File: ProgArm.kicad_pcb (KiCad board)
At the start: 2 copper layers, 40 x 70 mm, 103 parts, among them J1 MICROSD_SOCKET_SPI, M1 MOTOR, P1 I2C_Port, P2 I2C_Solder, P3 SPI_Port, P4 SPI_Solder, P5 JTAG_Interface, P6 Unused_Pins, P7 HC-05/06, P8 Ring_Port, P9 MicroUSB, Q1 MOS_P, Q10 MOS_P, Q11 MOS_P, Q12 MOS_P, Q2 MOS_N, Q3 MOS_N, Q4 MOS_P, Q5 MOS_P, Q6 MOS_P, Q7 MOS_P, Q8 MOS_P, Q9 MOS_P, SW1 ON/OFF, SW2 SWITCH_INV, U1 STM32F103R, U2 LTC2942-1, U3 BMP085, U4 HMC5883L, U5 MPU6050, X1 32.768(MS3V-T1R), X2 8 mHz

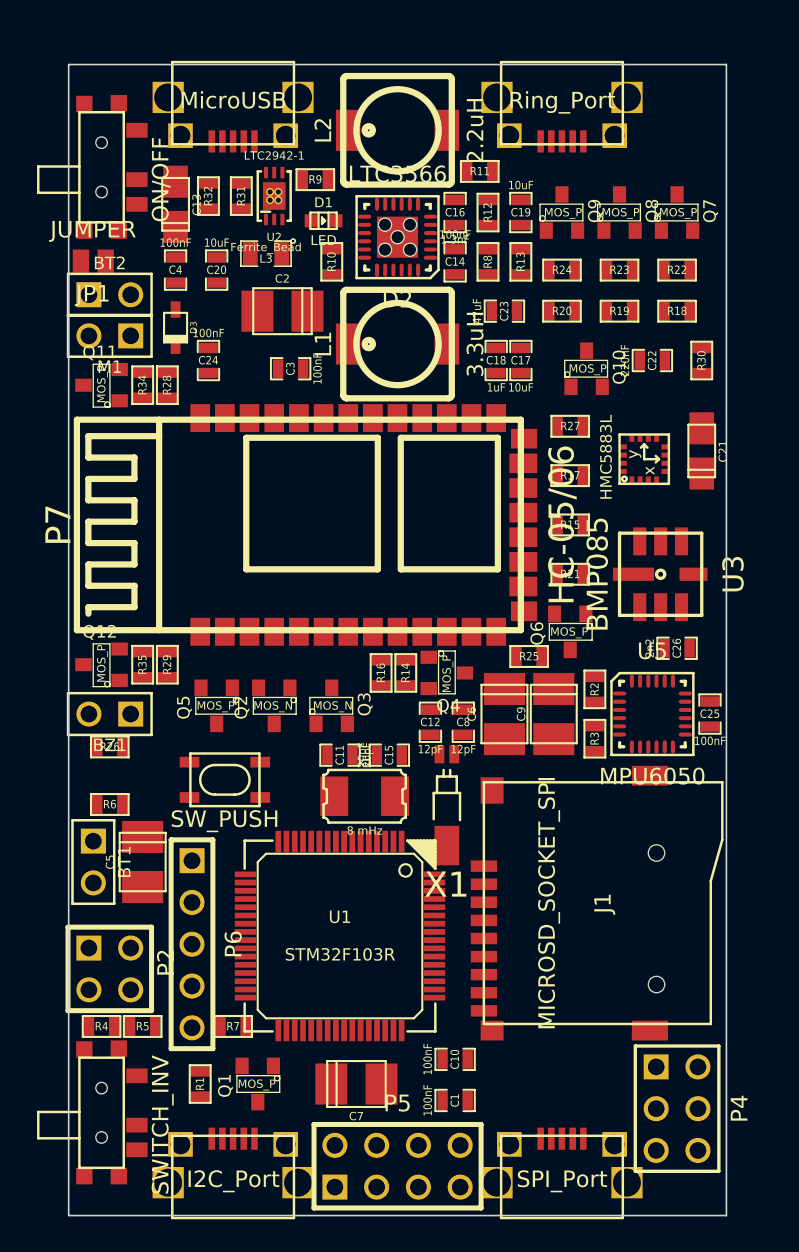
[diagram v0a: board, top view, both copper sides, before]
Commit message: Rearranged components
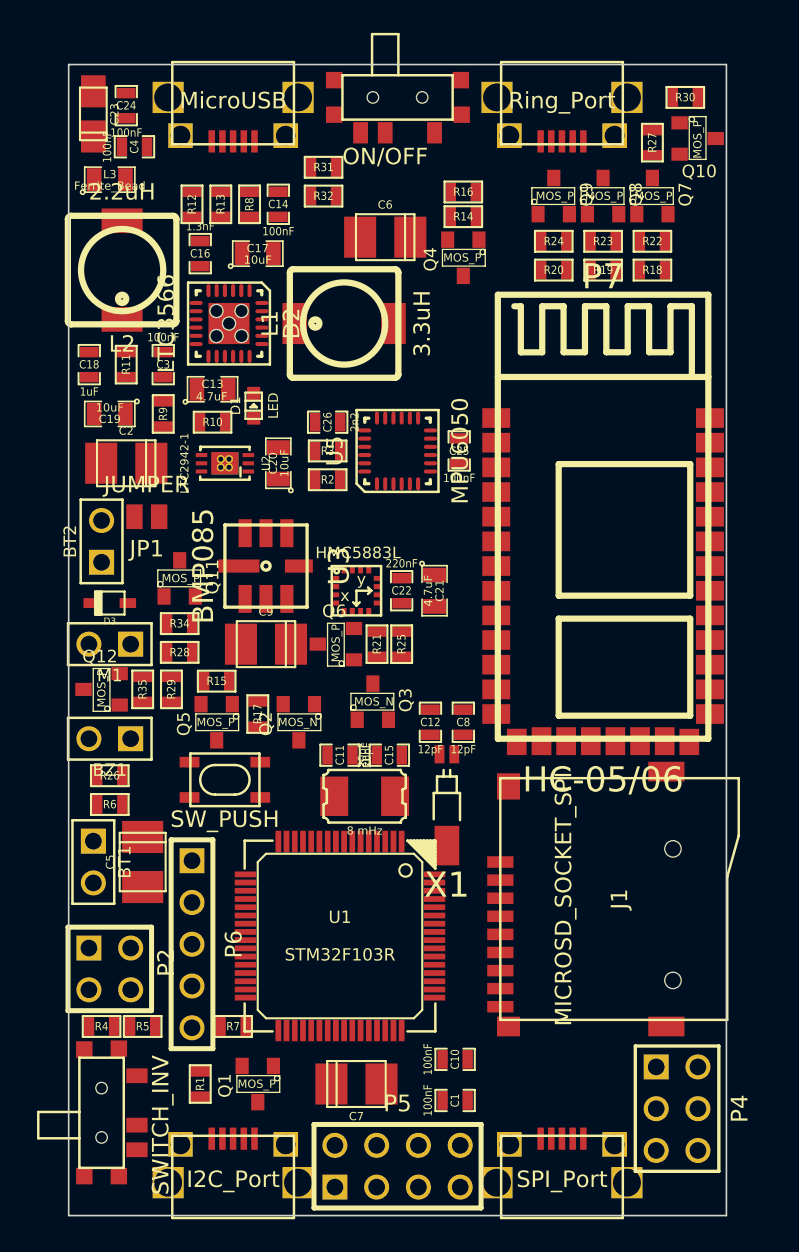
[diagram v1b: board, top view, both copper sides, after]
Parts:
- C13, C21: footprint c_tant_A -> SM0805
- C17, C19, C20: footprint SM0603_Capa -> SM0805
- C23: footprint SM0603_Capa -> c_tant_A
- moved C6 29.9 mm to (144.2, 60.5), turned to 0 degrees
- moved R16 29.7 mm to (149.0, 57.8), turned to 0 degrees
- moved R14 28.0 mm to (149.0, 59.2), turned to 0 degrees
- moved C19 27.8 mm to (127.5, 71.2), turned to 180 degrees
- moved C23 27.7 mm to (126.5, 53.0), turned to 270 degrees
- moved C26 25.3 mm to (140.8, 71.8), turned to 180 degrees
- moved Q4 25.3 mm to (149.0, 61.8), turned to 180 degrees
- moved C18 24.8 mm to (126.2, 68.2)
- moved R11 24.5 mm to (128.5, 68.2), turned to 90 degrees
- moved U3 24.0 mm to (137.0, 80.5)
- moved R17 23.9 mm to (136.5, 89.5), turned to 90 degrees
- moved R3 23.9 mm to (140.8, 73.5), turned to 0 degrees
- moved R15 23.5 mm to (134.0, 87.5)
- moved U5 22.3 mm to (145.0, 73.5), turned to 90 degrees
- moved C25 22.1 mm to (148.8, 73.5)
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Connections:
- D2 pad : (no net) -> GND

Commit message: New board layout attempt
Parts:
- moved C25 39.3 mm to (146.5, 112.8), turned to 180 degrees
- moved U5 35.0 mm to (146.5, 108.5), turned to 0 degrees
- moved C26 33.0 mm to (146.5, 104.2)
- moved Q3 24.4 mm to (136.2, 112.0), turned to 270 degrees
- moved C9 23.1 mm to (138.8, 108.2), turned to 180 degrees
- moved C21 23.0 mm to (141.5, 104.2), turned to 0 degrees
- moved U4 22.9 mm to (137.0, 104.2), turned to 90 degrees
- moved R7 22.3 mm to (148.5, 90.8), turned to 270 degrees
- moved U1 22.3 mm to (142.5, 80.8), turned to 0 degrees
- moved Q2 22.1 mm to (140.5, 112.0), turned to 270 degrees
- moved U3 21.6 mm to (146.8, 99.8)
- moved R3 21.5 mm to (148.8, 93.5), turned to 180 degrees
- moved R1 21.3 mm to (131.2, 90.8)
- moved R2 21.3 mm to (148.8, 95.0), turned to 180 degrees
- moved C22 20.4 mm to (136.8, 100.5), turned to 0 degrees
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
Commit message: ---
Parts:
- moved U4 47.9 mm to (144.8, 57.0), turned to 270 degrees
- moved C25 47.6 mm to (149.5, 65.2)
- moved U5 47.1 mm to (149.5, 61.5)
- moved C26 46.6 mm to (149.5, 57.8)
- moved R26 46.4 mm to (163.5, 64.0), turned to 270 degrees
- moved C21 43.9 mm to (144.5, 60.5)
- moved BZ1 42.6 mm to (163.5, 68.2), turned to 270 degrees
- moved C22 40.2 mm to (140.5, 60.5), turned to 180 degrees
- moved C9 39.6 mm to (153.5, 71.5)
- moved Q12 38.5 mm to (160.5, 69.0), turned to 180 degrees
- moved R35 37.9 mm to (160.5, 66.2), turned to 180 degrees
- moved M1 37.6 mm to (163.5, 74.2), turned to 270 degrees
- moved R14 36.5 mm to (149.2, 95.8), turned to 270 degrees
- moved P6 35.7 mm to (158.5, 79.0), turned to 180 degrees
- moved R16 35.5 mm to (148.8, 93.2)
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
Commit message: ---
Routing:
- net GND: track 0.00 -> 457.3 mm, vias 0 -> 6
- net +3.3V: track 0.00 -> 351.8 mm, vias 0 -> 19
- net ~VIBRATION: track 0.00 -> 114.5 mm, vias 0 -> 10
- net D+: track 0.00 -> 93.3 mm, vias 0 -> 8
- net SYS_POWER: track 0.00 -> 92.3 mm, vias 0 -> 5
- net /~LED_R: track 0.00 -> 89.7 mm, vias 0 -> 6
- net /I2C_EXTRA2: track 0.00 -> 82.1 mm, vias 0 -> 6
- net RING_BTN1: track 0.00 -> 77.1 mm, vias 0 -> 2
- net SDA: track 0.00 -> 75.0 mm, vias 0 -> 5
- net ~SYS_PWR_ENABLE: track 0.00 -> 74.1 mm, vias 0 -> 4
- net Vout: track 0.00 -> 72.9 mm, vias 0 -> 4
- net /~LED_G: track 0.00 -> 71.0 mm, vias 0 -> 6
- net PORT_POWER: track 0.00 -> 70.5 mm, vias 0 -> 2
- net SCL: track 0.00 -> 70.0 mm, vias 0 -> 4
- net /SD_MISO: track 0.00 -> 69.3 mm, vias 0 -> 10
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
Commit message: ---
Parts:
- moved R14 23.4 mm to (152.2, 72.5), turned to 0 degrees
- moved R16 22.8 mm to (152.2, 70.8)
- moved Q4 21.4 mm to (152.2, 75.2), turned to 180 degrees
- moved C9 7.94 mm to (157.2, 64.5)
- moved C6 7.79 mm to (155.5, 72.0)
- moved R26 5.25 mm to (163.5, 58.8)
- moved R28 5.20 mm to (158.5, 70.8), turned to 270 degrees
- moved BZ1 5.00 mm to (163.5, 63.2)
- moved R34 4.60 mm to (160.2, 70.8), turned to 90 degrees
- moved Q12 2.80 mm to (163.0, 67.8), turned to 270 degrees
- moved Q11 2.51 mm to (158.8, 74.5), turned to 180 degrees
- moved R35 1.52 mm to (160.2, 67.8), turned to 270 degrees
- moved R29 1.06 mm to (158.5, 67.8)
- moved U1 1.03 mm to (141.8, 89.2)
- moved Q7 0.25 mm to (160.2, 58.0)
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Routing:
- net GND: track 457.3 -> 0.00 mm, vias 6 -> 0
- net +3.3V: track 351.8 -> 0.00 mm, vias 19 -> 0
- net ~VIBRATION: track 114.5 -> 0.00 mm, vias 10 -> 0
- net D+: track 93.3 -> 0.00 mm, vias 8 -> 0
- net SYS_POWER: track 92.3 -> 0.00 mm, vias 5 -> 0
- net /~LED_R: track 89.7 -> 0.00 mm, vias 6 -> 0
- net /I2C_EXTRA2: track 82.1 -> 0.00 mm, vias 6 -> 0
- net RING_BTN1: track 77.1 -> 0.00 mm, vias 2 -> 0
- net SDA: track 75.0 -> 0.00 mm, vias 5 -> 0
- net ~SYS_PWR_ENABLE: track 74.1 -> 0.00 mm, vias 4 -> 0
- net Vout: track 72.9 -> 0.00 mm, vias 4 -> 0
- net /~LED_G: track 71.0 -> 0.00 mm, vias 6 -> 0
- net PORT_POWER: track 70.5 -> 0.00 mm, vias 2 -> 0
- net SCL: track 70.0 -> 0.00 mm, vias 4 -> 0
- net /SD_MISO: track 69.3 -> 0.00 mm, vias 10 -> 0
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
